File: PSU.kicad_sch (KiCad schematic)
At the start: 87 parts, among them Q1 DMT6008LFG, U11 RT8293B, U12 USBLC6-2P6, U17 TPS2121RUXR, U19 TLV77333PDBVR, U20 TPS65133DPDR, U21 LM74700, U22 TLV77325PDBVR, U27 TLV77333PDBVR, U4 TPS7A39

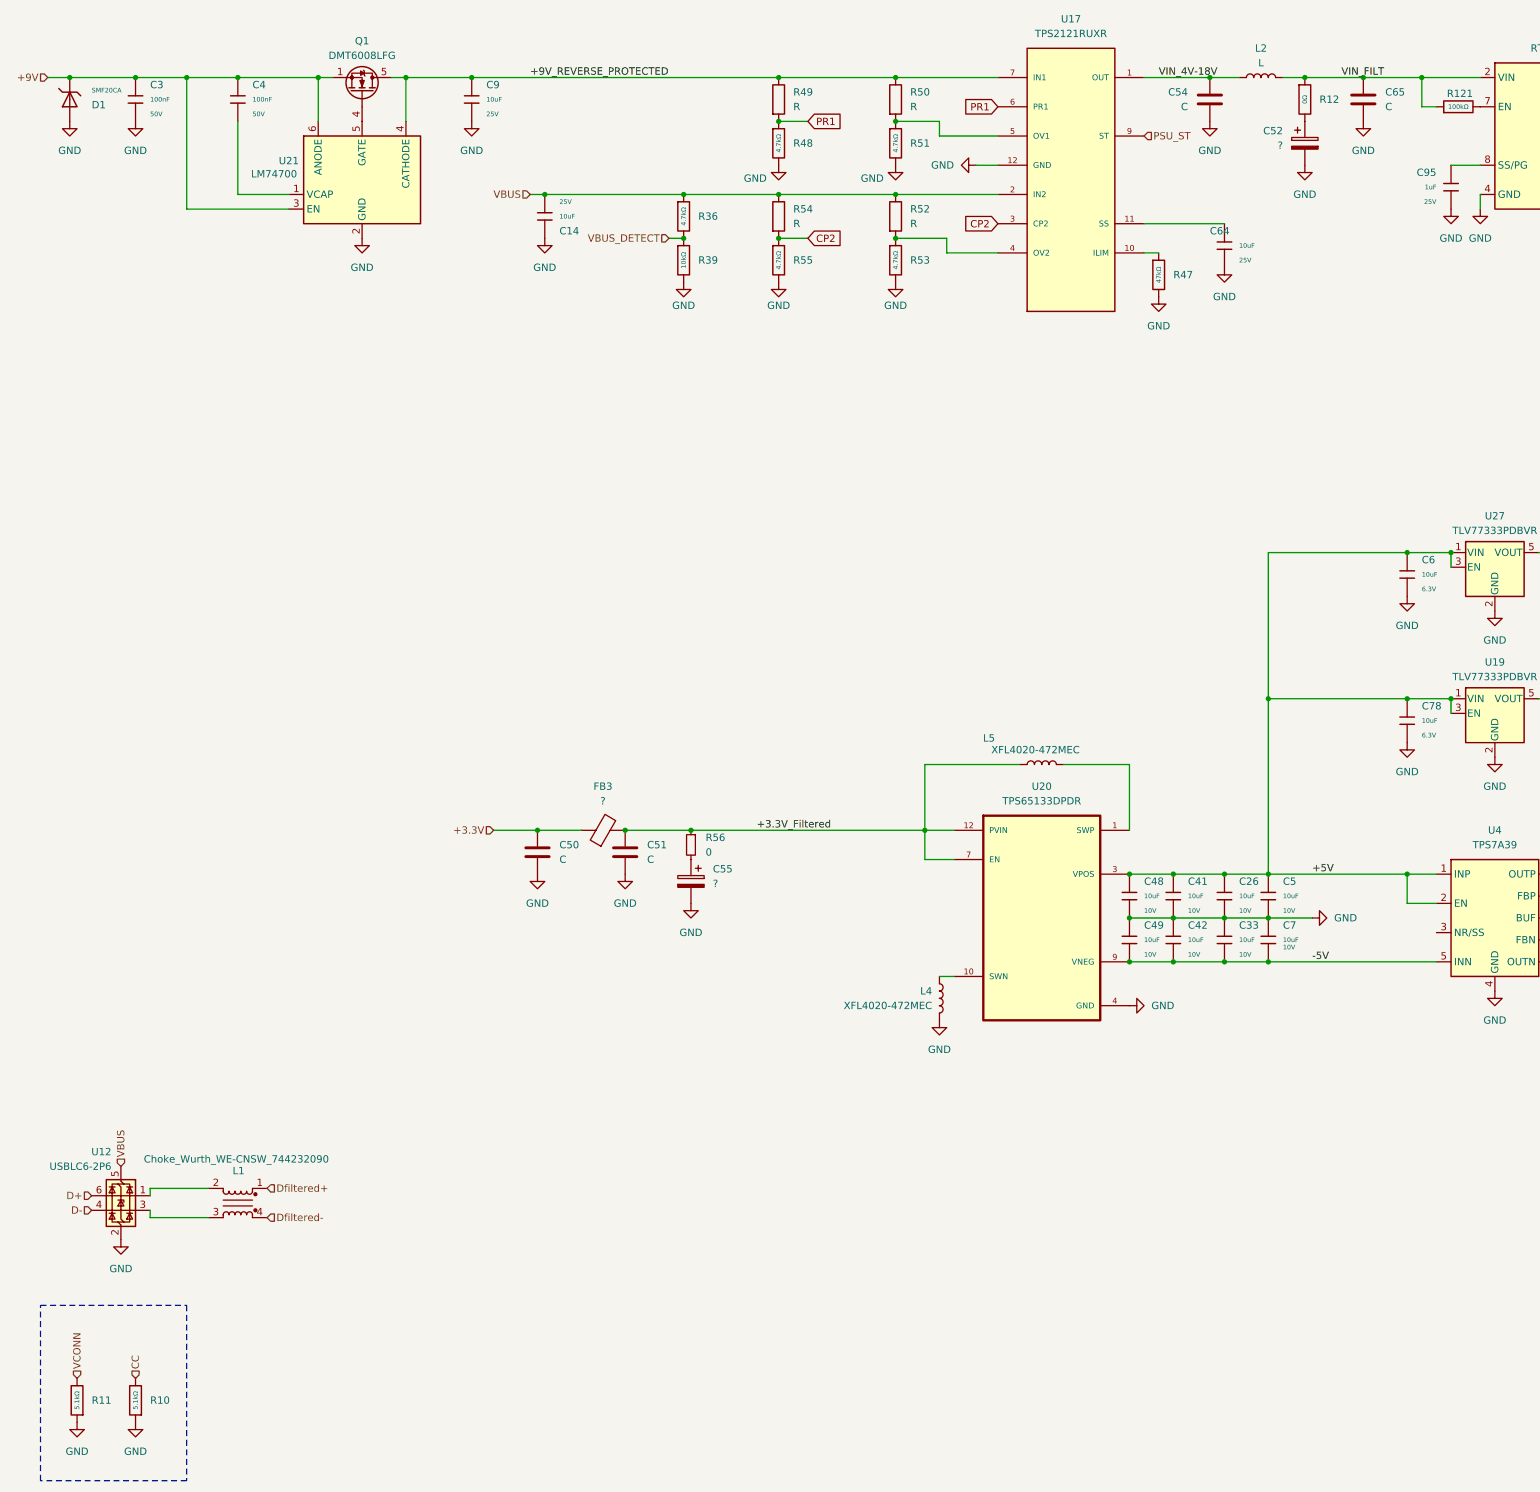
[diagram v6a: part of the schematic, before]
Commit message: deleted usb powering option because of 4.5V minimum input voltage of DC-DC
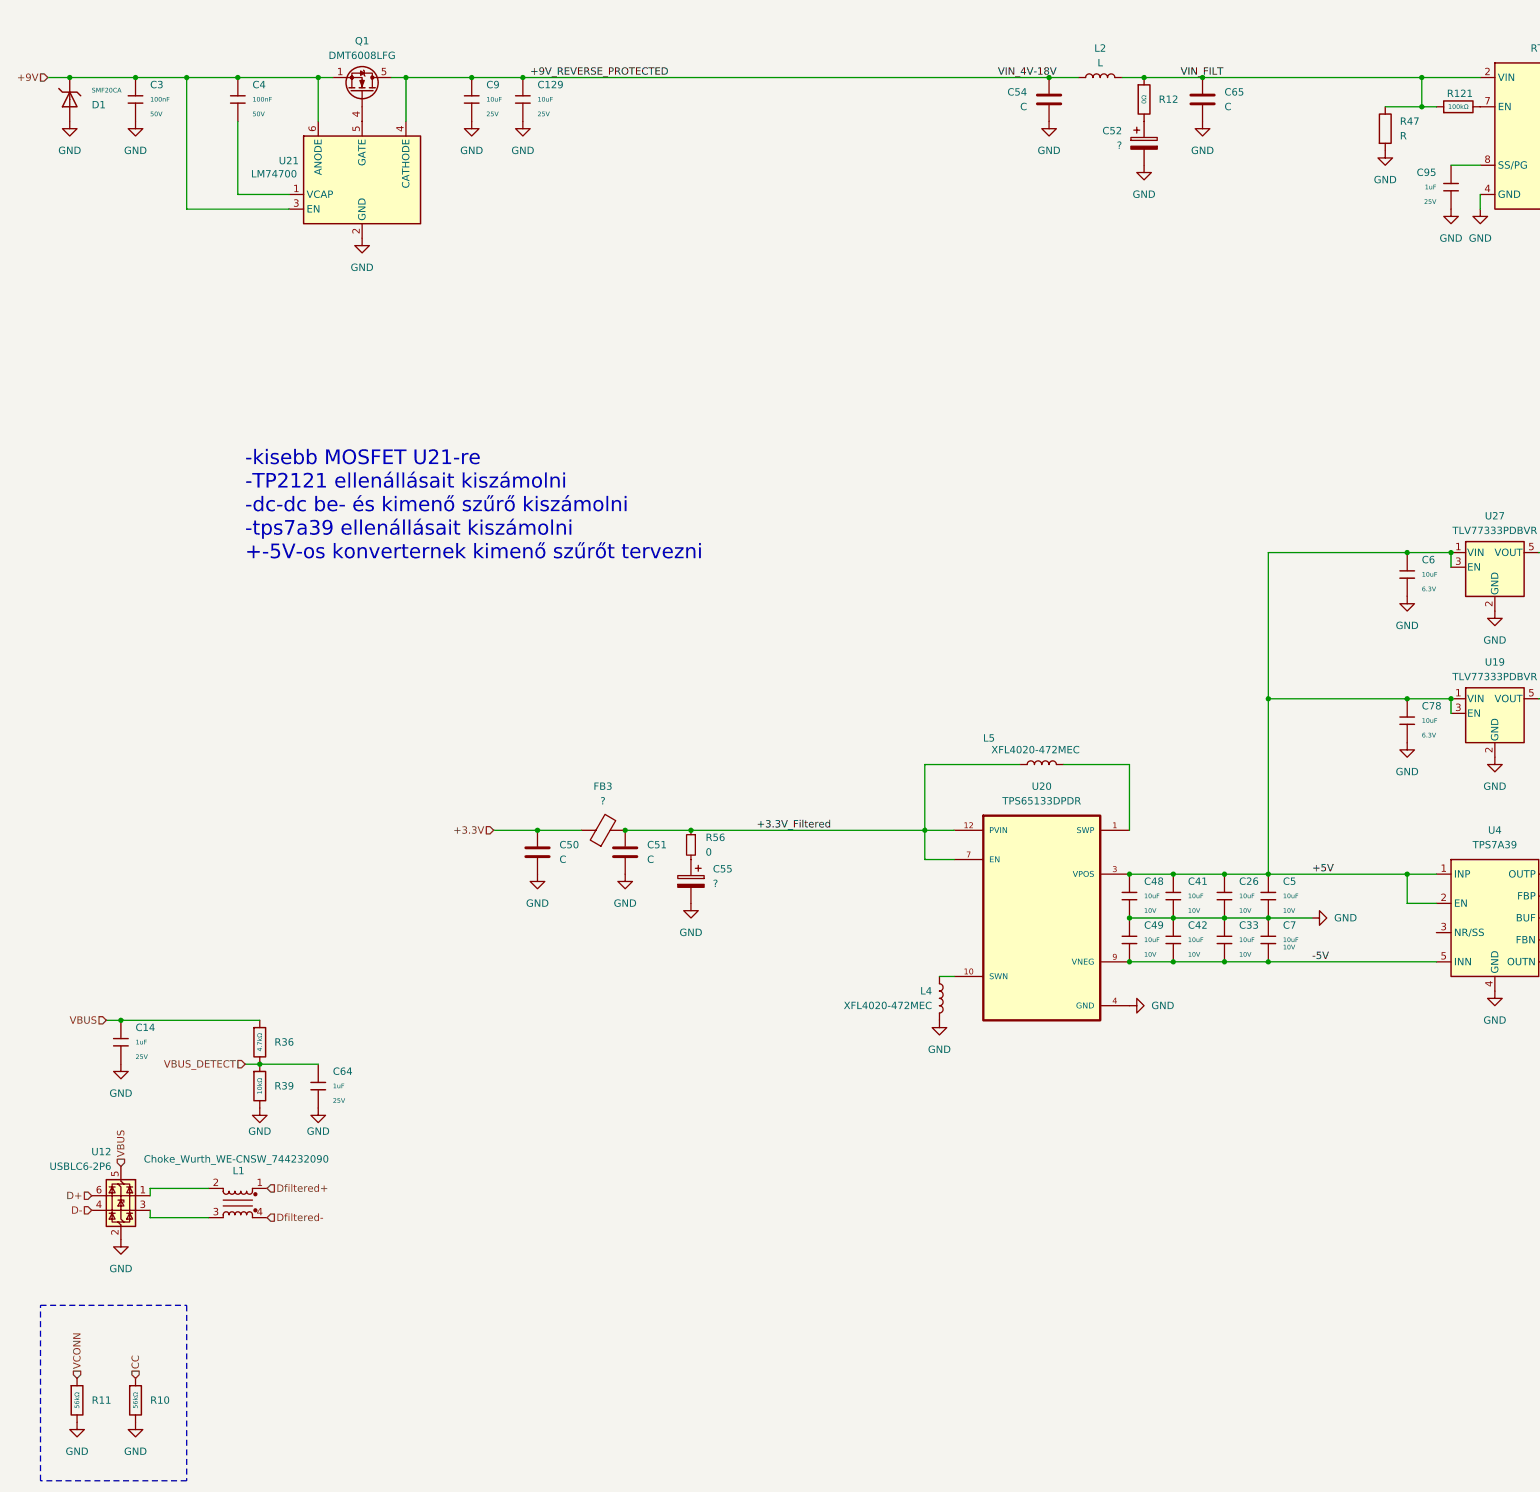
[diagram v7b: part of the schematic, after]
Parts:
- removed C14, C64: 10uF, PCM_JLCPCB:C_0603, symbol PCM_JLCPCB-Capacitors:0603,10uF,(2)
- removed R10, R11: 5.1kΩ, PCM_JLCPCB:R_0402, symbol PCM_JLCPCB-Resistors:0402,5.1kΩ
- removed R47: 47kΩ, PCM_JLCPCB:R_0402, symbol PCM_JLCPCB-Resistors:0402,47kΩ
- removed R48, R51, R53, R55: 4.7kΩ, PCM_JLCPCB:R_0603, symbol PCM_JLCPCB-Resistors:0603,4.7kΩ
- removed R49, R50, R52, R54: R, symbol Device:R
- removed U17: TPS2121RUXR, User:IC_TPS2121RUXR, symbol User:TPS2121RUXR
- added C129: 10uF, PCM_JLCPCB:C_0603, symbol PCM_JLCPCB-Capacitors:0603,10uF,(2)
- added C14, C64: 1uF, PCM_JLCPCB:C_0402, symbol PCM_JLCPCB-Capacitors:0402,1uF
- added R10, R11: 56kΩ, PCM_JLCPCB:R_0402, symbol PCM_JLCPCB-Resistors:0402,56kΩ
- added R47: R, symbol Device:R
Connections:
- net VIN_4V-18V is gone; now on net +9V_REVERSE_PROTECTED: C54.1, L2.1
- net +9V_REVERSE_PROTECTED: now also C129.1
- net AGND: now also C129.2, C14.2, C64.2, R10.2, R11.2, R47.2
- net CC: now also R10.1
- net VBUS: now also C14.1
- net VBUS_DETECT: now also C64.1
- net VCONN: now also R11.1
- net VIN_FILT: now also R47.1
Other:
- note added: "-kisebb MOSFET U21-re -TP2121 ellenállásait kiszámolni -dc-dc be- és kimenő szűrő kiszámolni -tps7a39 ellenállásait kiszámolni +-5V-os konverternek kimenő szűrőt tervezni"
- moved on the sheet: C52, C54, C65, L2, R12, R36, R39

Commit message: lot of changes
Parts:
- removed C14, C64: 1uF, PCM_JLCPCB:C_0402, symbol PCM_JLCPCB-Capacitors:0402,1uF
- removed C25, C6, C78, C96: 10uF, PCM_JLCPCB:C_0402, symbol PCM_JLCPCB-Capacitors:0402,10uF
- removed C4: 100nF, PCM_JLCPCB:C_0402, symbol PCM_JLCPCB-Capacitors:0402,100nF,(2)
- removed C9: 10uF, PCM_JLCPCB:C_0603, symbol PCM_JLCPCB-Capacitors:0603,10uF,(2)
- removed L1: Choke_Wurth_WE-CNSW_744232090, Inductor_SMD:L_CommonMode_Wurth_WE-CNSW-1206, symbol Filter:Choke_Wurth_WE-CNSW_744232090
- removed L4, L5: XFL4020-472MEC, Inductor_SMD:L_Coilcraft_XxL4020, symbol Device:L
- removed Q1: DMT6008LFG, Package_SON:Diodes_PowerDI3333-8, symbol Transistor_FET:DMT6008LFG
- removed R10, R11: 56kΩ, PCM_JLCPCB:R_0402, symbol PCM_JLCPCB-Resistors:0402,56kΩ
- removed R36: 4.7kΩ, PCM_JLCPCB:R_0402, symbol PCM_JLCPCB-Resistors:0402,4.7kΩ
- removed R39, R57: 10kΩ, PCM_JLCPCB:R_0402, symbol PCM_JLCPCB-Resistors:0402,10kΩ
- removed R47: R, symbol Device:R
- removed U12: USBLC6-2P6, Package_TO_SOT_SMD:SOT-666, symbol Power_Protection:USBLC6-2P6
- removed U19, U27: TLV77333PDBVR, Package_TO_SOT_SMD:SOT-23-5, symbol Regulator_Linear:AP2127K-3.3
- removed U20: TPS65133DPDR, User:SON40P300X300X80-13N, symbol User:TPS65133DPDR
- removed U21: LM74700, Package_TO_SOT_SMD:SOT-23-6, symbol Power_Management:LM74700
- added C24: 4.7uF, PCM_JLCPCB:C_0805, symbol PCM_JLCPCB-Capacitors:0805,4.7uF
- added C4: 1uF, PCM_JLCPCB:C_0402, symbol PCM_JLCPCB-Capacitors:0402,1uF
- added C6, C9: 100nF, PCM_JLCPCB:C_0402, symbol PCM_JLCPCB-Capacitors:0402,100nF,(2)
- added D3: SMF20CA, PCM_JLCPCB:D_SOD-123FL, symbol PCM_JLCPCB-Diodes:TVS-Uni,SMF20CA
- added L3: 33u, symbol Device:L
- added R119: 110k, Resistor_SMD:R_0402_1005Metric, symbol Device:R_Small
- added R120: 8.2k, Resistor_SMD:R_0402_1005Metric, symbol Device:R_Small
- added R130: 12k, Resistor_SMD:R_0402_1005Metric, symbol Device:R_Small
- added R131: 20k, Resistor_SMD:R_0402_1005Metric, symbol Device:R_Small
- added R3: 47Ω, PCM_JLCPCB:R_0402, symbol PCM_JLCPCB-Resistors:0402,47Ω
- added R31: 24kΩ, PCM_JLCPCB:R_0402, symbol PCM_JLCPCB-Resistors:0402,24kΩ
- added R6: 4.3kΩ, PCM_JLCPCB:R_0603, symbol PCM_JLCPCB-Resistors:0603,4.3kΩ
- added U14: TPS26400PWPR, User:PWP0016H-IPC_A, symbol 2025-02-23_17-32-12:TPS26400PWPR
- added U5: TPS560430XFDBVT, Package_TO_SOT_SMD:SOT-23-6, symbol User:TPS560430XF
- C30: renamed from C80; now not fitted
- L4: renamed from L3; footprint (none) -> Inductor_SMD:L_Cenker_CKCS8040
- U10: renamed from U11; footprint (none) -> Package_SO:TI_SO-PowerPAD-8
- renumbered C95 to C25, C63 to C27, C57 to C28, C24 to C29, C58 to C35, C59 to C57, C60 to C63, C61 to C80, C62 to C85, R121 to R32, R46 to R33, R119 to R34, R98 to R46, R120 to R47
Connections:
- net +3.3V: no longer C50.1, FB3.1
- net +9V: now also D3.1, R119.1, U14.1 (IN), U14.2 (IN)
- net +4.5V renamed +V_OPA
- net +5V: no longer names the net of C26.1, C41.1, C48.1, C5.1, U4.1 (INP)
- net +5V: no longer U4.2 (EN)
- net +9V_REVERSE_PROTECTED: no longer names the net of C54.1, L2.1
- net +9V_REVERSE_PROTECTED: no longer C129.1
- net -4.5V renamed -V_OPA
- net -5V renamed -7V
- net -7V: now also C24.2, C6.2, R6.2, U5.2 (GND)
- net AGND renamed GND
- net GND: now also C24.1, L3.2, R3.2, U14.9 (GND)
- net AVIN: no longer names the net of C51.1, FB3.2, R56.1
- net VIN_FILT renamed +9-18V
- net +9-18V: no longer R32.1, U10.2 (VIN)
- new net: R131.1, U14.11 (ILIM)
- new net: C4.1, U14.12 (dVdT)
- new net: C129.1, D3.2, U14.15 (OUT), U14.16 (OUT)
- new net: R119.2, R120.1, U14.3 (UVLO)
- new net: R120.2, R130.1, U14.5 (OVP)
- new net: C50.1, FB3.1
- new net: R32.1, U10.2 (VIN)
- new net: C9.1, U5.1 (CB)
- new net: R31.1, R6.1, U5.3 (FB)
- new net: C6.1, U5.4 (EN), U5.5 (VIN)
- new net: C9.2, L3.1, U5.6 (SW)
- new net: R3.1, R31.2
- new net PowerPad: C4.2, R130.2, R131.2, U14.17 (PowerPAD), U14.8 (RTN)
- no-connect marks 0 -> 6
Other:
- note added: "OMRON G6K-2F-Y-TR DC5"
- note added: "https://www.ti.com/lit/an/slvae10/slvae10.pdf?utm_source=chatgpt.com&ts=1755168580112&ref_url=https%253A%252F%252Fchatgpt.com%252F"
- moved on the sheet: C106, C107, C108, C109, C110, C111, C129, C25, C26, C27, C28, C29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
